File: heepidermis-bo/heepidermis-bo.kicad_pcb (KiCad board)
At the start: 4 copper layers, 85.7 x 54 mm, 10 parts

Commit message: Finished ADC/DAC board
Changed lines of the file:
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@@
 		)
 		(fp_text user "${REFERENCE}"
-			(at 0.635 9.525 360)
+			(at 0.635 9.525 0)
 			(layer "F.Fab")
 			(effects
@@
 		)
 		(property "Footprint" "heep_footprints:EPFL"
-			(at 0 0 360)
+			(at 0 0 0)
 			(layer "F.Fab")
 			(hide yes)
@@
 		)
 		(property "Datasheet" ""
-			(at 0 0 360)
+			(at 0 0 0)
 			(layer "F.Fab")
 			(hide yes)
@@
 		)
 		(property "Description" ""
-			(at 0 0 360)
+			(at 0 0 0)
 			(layer "F.Fab")
 			(hide yes)
@@
 		)
 		(fp_text user "${REFERENCE}"
-			(at 1.27 11.43 360)
+			(at 1.27 11.43 0)
 			(layer "F.Fab")
 			(effects
@@
 		)
 		(property "Footprint" "heep_footprints:ESL"
-			(at 0 0 360)
+			(at 0 0 0)
 			(layer "F.Fab")
 			(hide yes)
@@
 		)
 		(property "Datasheet" ""
-			(at 0 0 360)
+			(at 0 0 0)
 			(layer "F.Fab")
 			(hide yes)
@@
 		)
 		(property "Description" ""
-			(at 0 0 360)
+			(at 0 0 0)
 			(layer "F.Fab")
 			(hide yes)
@@
 		(width 0.25)
 		(layer "B.Cu")
+		(net 13)
+	)
+	(segment
+		(start 140.5285 116.8485)
+		(end 140.74 117.06)
+		(width 0.25)
+		(layer "B.Cu")
+		(net 13)
+	)
+	(segment
+		(start 140.5285 116.75)
+		(end 140.5285 116.8485)
+		(width 0.25)
+		(layer "B.Cu")

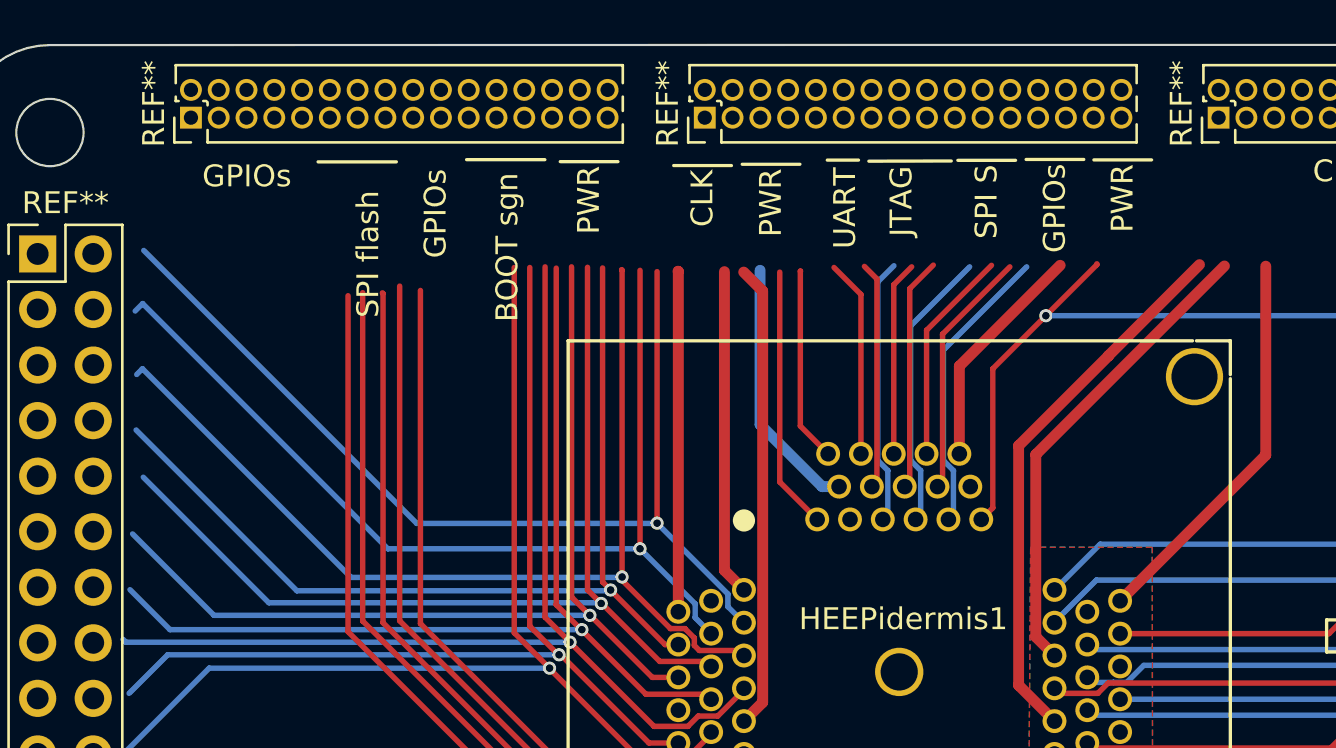
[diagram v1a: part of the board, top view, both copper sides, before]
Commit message: Before re-routing programmer
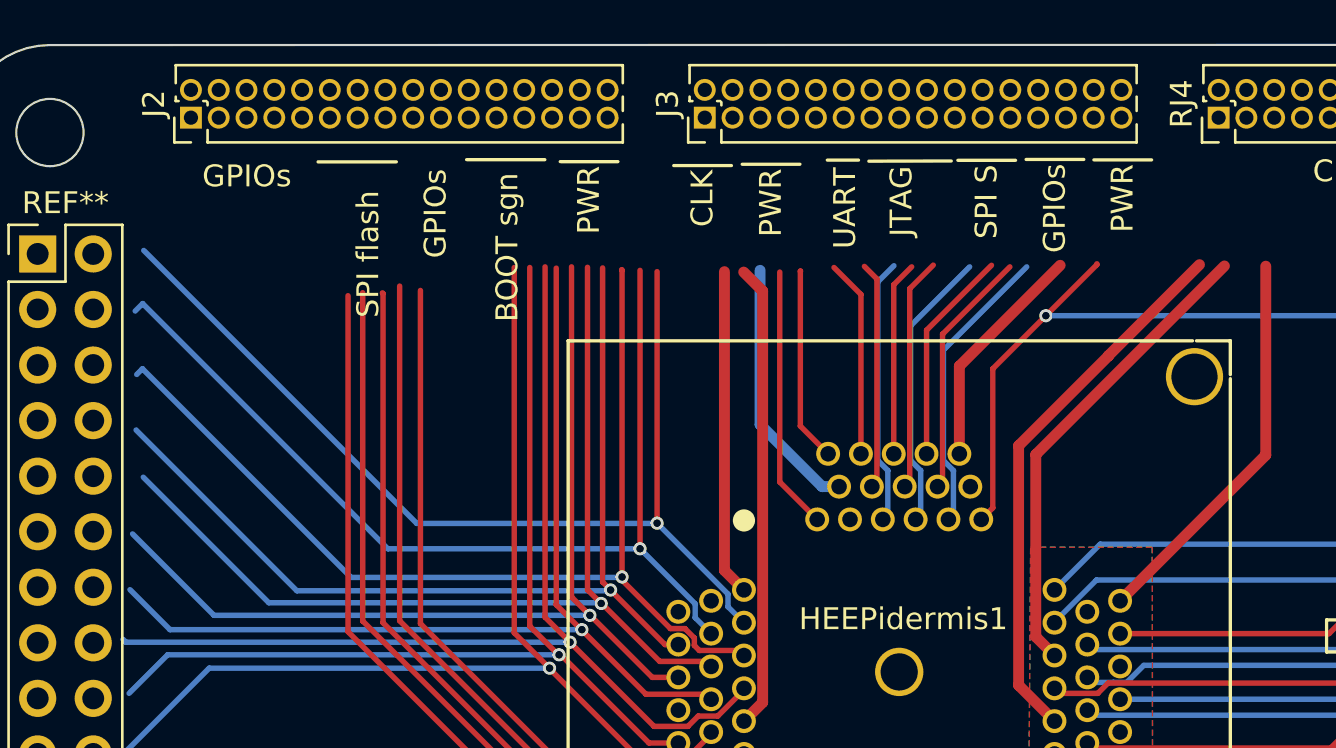
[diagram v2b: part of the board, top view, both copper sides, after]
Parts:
- renumbered REF** to J2, REF** to J3, REF** to RJ4
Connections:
- HEEPidermis1 pad 3: /DCORE_VDD -> unconnected-(HEEPidermis1-Pad3)
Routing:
- net /DCORE_VDD: track 26.1 -> 10.5 mm
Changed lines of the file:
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@@
 	(net 55 "unconnected-(HEEPidermis1-Pad66)")
 	(net 56 "unconnected-(HEEPidermis1-Pad65)")
+	(net 57 "unconnected-(HEEPidermis1-Pad3)")
 	(footprint "Connector_PinHeader_1.27mm:PinHeader_2x16_P1.27mm_Vertical"
 		(layer "F.Cu")
@@
 		(descr "Through hole straight pin header, 2x16, 1.27mm pitch, double rows")
 		(tags "Through hole pin header THT 2x16 1.27mm double row")
-		(property "Reference" "REF**"
+		(property "Reference" "J2"
 			(at 0.635 -1.695 90)
 			(layer "F.SilkS")
@@
 		(descr "Through hole straight pin header, 2x16, 1.27mm pitch, double rows")
 		(tags "Through hole pin header THT 2x16 1.27mm double row")
-		(property "Reference" "REF**"
+		(property "Reference" "RJ4"
 			(at 0.635 -1.695 90)
 			(layer "F.SilkS")
@@
 			)
 			(remove_unused_layers no)
-			(net 31 "/DCORE_VDD")
+			(net 57 "unconnected-(HEEPidermis1-Pad3)")
 			(pinfunction "3")
-			(pintype "unspecified")
+			(pintype "unspecified+no_connect")
 			(clearance 0.05)
 		)
@@
 		(descr "Through hole straight pin header, 2x16, 1.27mm pitch, double rows")
 		(tags "Through hole pin header THT 2x16 1.27mm double row")
-		(property "Reference" "REF**"
+		(property "Reference" "J3"
 			(at 0.635 -1.695 90)
 			(layer "F.SilkS")
@@
 	)
 	(segment
-		(start 126.1515 81.213)
-		(end 126.1385 81.2)
-		(width 0.5)
-		(layer "F.Cu")
-		(net 31)
-	)
-	(segment
 		(start 139 85.5385)
 		(end 143.6085 80.93)
 		(width 0.5)
 		(layer "F.Cu")
-		(net 31)
-	)
-	(segment
-		(start 126.1515 96.770001)
-		(end 126.1515 81.213)
-		(width 0.5)
-		(layer "F.Cu")
